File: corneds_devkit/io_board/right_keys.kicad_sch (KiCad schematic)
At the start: 42 parts, among them SW14 SW_Push, SW16 SW_Push, SW18 SW_Push, SW25 SW_Push, SW26 SW_Push, SW27 SW_Push, SW28 SW_Push, SW29 SW_Push, SW30 SW_Push, SW31 SW_Push, SW32 SW_Push, SW33 SW_Push, SW34 SW_Push, SW35 SW_Push, SW36 SW_Push, SW37 SW_Push, SW38 SW_Push, SW39 SW_Push, SW40 SW_Push, SW41 SW_Push, SW42 SW_Push

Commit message: routing left keys pcb
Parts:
- SW14, SW16, SW18, SW25, SW26, SW27, SW28, SW29, SW30, SW31, SW32, SW33, SW34, SW35, SW36, SW37, SW38, SW39, SW40, SW41, SW42: footprint key-switches:SW_Gateron_LowProfile_HotSwap_THT -> key-switches:SW_Gateron_LowProfile_HotSwap_PTH
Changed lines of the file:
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@@
 			)
 		)
-		(property "Footprint" "key-switches:SW_Gateron_LowProfile_HotSwap_THT"
+		(property "Footprint" "key-switches:SW_Gateron_LowProfile_HotSwap_PTH"
 			(at 128.27 34.29 0)
 			(effects
@@
 			)
 		)
-		(property "Footprint" "key-switches:SW_Gateron_LowProfile_HotSwap_THT"
+		(property "Footprint" "key-switches:SW_Gateron_LowProfile_HotSwap_PTH"
 			(at 100.33 130.81 0)
 			(effects
@@
 			)
 		)
-		(property "Footprint" "key-switches:SW_Gateron_LowProfile_HotSwap_THT"
+		(property "Footprint" "key-switches:SW_Gateron_LowProfile_HotSwap_PTH"
 			(at 72.39 34.29 0)
 			(effects
@@
 			)
 		)
-		(property "Footprint" "key-switches:SW_Gateron_LowProfile_HotSwap_THT"
+		(property "Footprint" "key-switches:SW_Gateron_LowProfile_HotSwap_PTH"
 			(at 72.39 99.06 0)
 			(effects
@@
 			)
 		)
-		(property "Footprint" "key-switches:SW_Gateron_LowProfile_HotSwap_THT"
+		(property "Footprint" "key-switches:SW_Gateron_LowProfile_HotSwap_PTH"
 			(at 156.21 34.29 0)
 			(effects
@@
 			)
 		)
-		(property "Footprint" "key-switches:SW_Gateron_LowProfile_HotSwap_THT"
+		(property "Footprint" "key-switches:SW_Gateron_LowProfile_HotSwap_PTH"
 			(at 100.33 66.04 0)
 			(effects
@@
 			)
 		)
-		(property "Footprint" "key-switches:SW_Gateron_LowProfile_HotSwap_THT"
+		(property "Footprint" "key-switches:SW_Gateron_LowProfile_HotSwap_PTH"
 			(at 128.27 66.04 0)
 			(effects
@@
 			)
 		)
-		(property "Footprint" "key-switches:SW_Gateron_LowProfile_HotSwap_THT"
+		(property "Footprint" "key-switches:SW_Gateron_LowProfile_HotSwap_PTH"
 			(at 100.33 99.06 0)
 			(effects
@@
 			)
 		)
-		(property "Footprint" "key-switches:SW_Gateron_LowProfile_HotSwap_THT"
+		(property "Footprint" "key-switches:SW_Gateron_LowProfile_HotSwap_PTH"
 			(at 212.09 34.29 0)
 			(effects
@@
 			)
 		)
-		(property "Footprint" "key-switches:SW_Gateron_LowProfile_HotSwap_THT"
+		(property "Footprint" "key-switches:SW_Gateron_LowProfile_HotSwap_PTH"
 			(at 212.09 99.06 0)
 			(effects
@@
 			)
 		)
-		(property "Footprint" "key-switches:SW_Gateron_LowProfile_HotSwap_THT"
+		(property "Footprint" "key-switches:SW_Gateron_LowProfile_HotSwap_PTH"
 			(at 184.15 99.06 0)
 			(effects
@@
 			)
 		)
-		(property "Footprint" "key-switches:SW_Gateron_LowProfile_HotSwap_THT"
+		(property "Footprint" "key-switches:SW_Gateron_LowProfile_HotSwap_PTH"
 			(at 128.27 99.06 0)
 			(effects
@@
 			)
 		)
-		(property "Footprint" "key-switches:SW_Gateron_LowProfile_HotSwap_THT"
+		(property "Footprint" "key-switches:SW_Gateron_LowProfile_HotSwap_PTH"
 			(at 184.15 34.29 0)
 			(effects
@@
 			)
 		)
-		(property "Footprint" "key-switches:SW_Gateron_LowProfile_HotSwap_THT"
+		(property "Footprint" "key-switches:SW_Gateron_LowProfile_HotSwap_PTH"
 			(at 212.09 66.04 0)
 			(effects
@@
 			)
 		)
-		(property "Footprint" "key-switches:SW_Gateron_LowProfile_HotSwap_THT"
+		(property "Footprint" "key-switches:SW_Gateron_LowProfile_HotSwap_PTH"
 			(at 100.33 34.29 0)
 			(effects
@@
 			)
 		)
-		(property "Footprint" "key-switches:SW_Gateron_LowProfile_HotSwap_THT"
+		(property "Footprint" "key-switches:SW_Gateron_LowProfile_HotSwap_PTH"
 			(at 184.15 66.04 0)
 			(effects
@@
 			)
 		)
-		(property "Footprint" "key-switches:SW_Gateron_LowProfile_HotSwap_THT"
+		(property "Footprint" "key-switches:SW_Gateron_LowProfile_HotSwap_PTH"
 			(at 128.27 130.81 0)
 			(effects
@@
 			)
 		)
-		(property "Footprint" "key-switches:SW_Gateron_LowProfile_HotSwap_THT"
+		(property "Footprint" "key-switches:SW_Gateron_LowProfile_HotSwap_PTH"
 			(at 156.21 99.06 0)
 			(effects
@@
 			)
 		)
-		(property "Footprint" "key-switches:SW_Gateron_LowProfile_HotSwap_THT"
+		(property "Footprint" "key-switches:SW_Gateron_LowProfile_HotSwap_PTH"
 			(at 72.39 130.81 0)
 			(effects
@@
 			)
 		)
-		(property "Footprint" "key-switches:SW_Gateron_LowProfile_HotSwap_THT"
+		(property "Footprint" "key-switches:SW_Gateron_LowProfile_HotSwap_PTH"
 			(at 72.39 66.04 0)
 			(effects
@@
 			)
 		)
-		(property "Footprint" "key-switches:SW_Gateron_LowProfile_HotSwap_THT"
+		(property "Footprint" "key-switches:SW_Gateron_LowProfile_HotSwap_PTH"
 			(at 156.21 66.04 0)
 			(effects

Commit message: finished io board
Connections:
- net rclick_led_di: now also D78.1 (DO); no longer D64.1 (DO)
- net right_led_di: now also D77.4 (DI); no longer D26.4 (DI)
- net at D79.1 (DO): now also D71.4 (DI); no longer D80.4 (DI)
- net at D71.1 (DO): now also D63.4 (DI); no longer D79.4 (DI)
- net at D72.1 (DO): now also D80.4 (DI); no longer D64.4 (DI)
- net at D72.4 (DI): now also D64.1 (DO); no longer D80.1 (DO)
- net at D50.1 (DO): now also D56.4 (DI); no longer D28.4 (DI)
- net at D50.4 (DI): now also D28.1 (DO); no longer D56.1 (DO)
- net at D30.4 (DI): now also D51.1 (DO); no longer D28.1 (DO)
- net at D63.1 (DO): now also D57.4 (DI); no longer D71.4 (DI)
- net at D57.1 (DO): now also D51.4 (DI); no longer D63.4 (DI)
- net at D70.4 (DI): now also D62.1 (DO); no longer D78.1 (DO)
- net at D78.4 (DI): now also D70.1 (DO); no longer D77.1 (DO)
- net at D61.1 (DO): now also D55.4 (DI); no longer D69.4 (DI)
- net at D61.4 (DI): now also D69.1 (DO); no longer D55.1 (DO)
- net at D49.1 (DO): now also D26.4 (DI); no longer D55.4 (DI)
- net at D26.1 (DO): now also D28.4 (DI); no longer D49.4 (DI)
- net at D30.1 (DO): now also D64.4 (DI); no longer D51.4 (DI)
- net at D62.4 (DI): now also D56.1 (DO); no longer D70.1 (DO)
- new net: D69.4 (DI), D77.1 (DO)
- new net: D49.4 (DI), D55.1 (DO)
- new net rclick_led_do: D79.4 (DI)

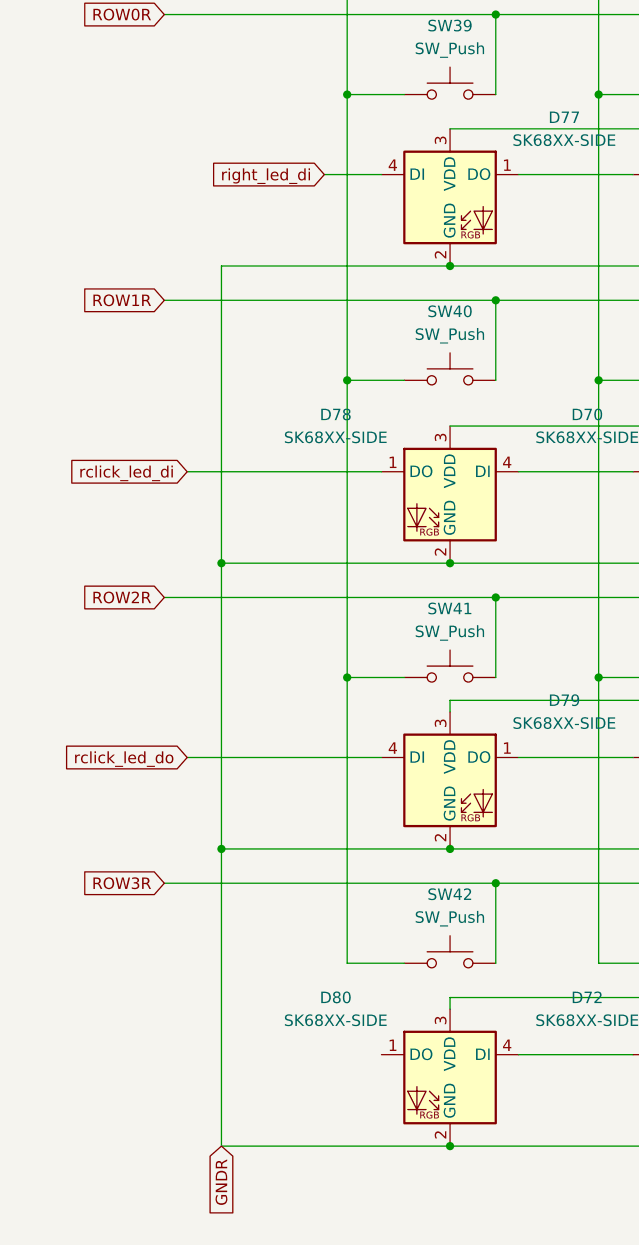
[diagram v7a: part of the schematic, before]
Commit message: finished routing power board and started on control board schematic but realized I need seperate reset lines
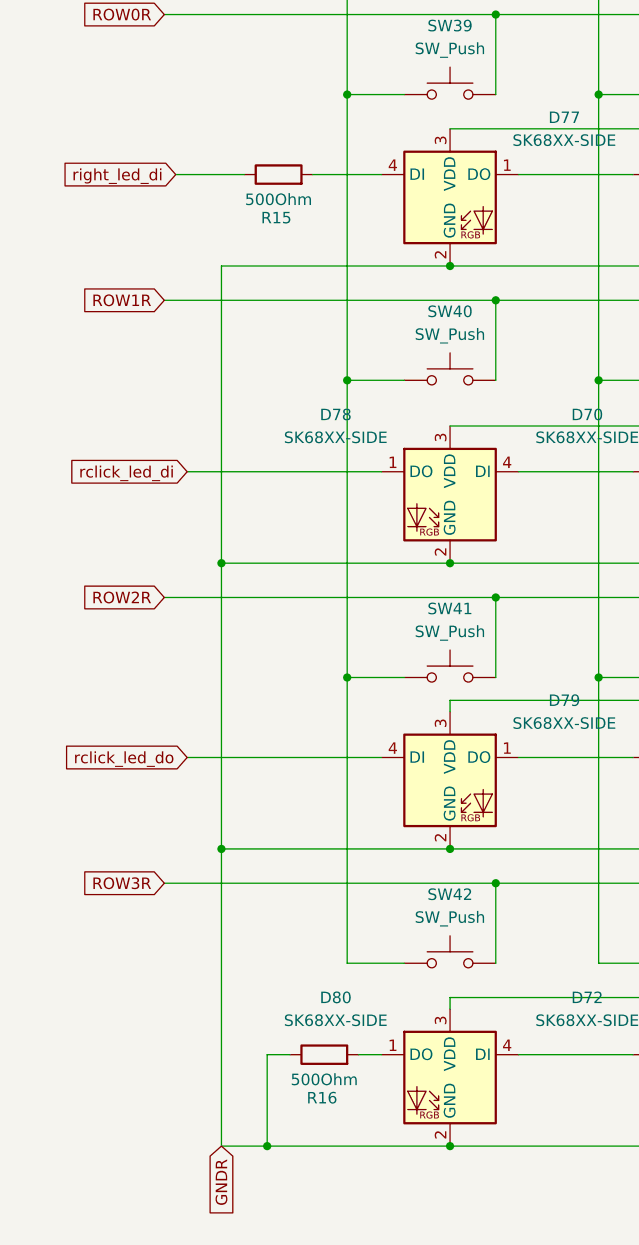
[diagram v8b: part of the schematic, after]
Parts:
- added R15, R16: 500Ohm, Resistor_SMD:R_0402_1005Metric, symbol Device:R
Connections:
- net GNDR: now also R16.1
- net right_led_di: now also R15.1; no longer D77.4 (DI)
- net at D80.1 (DO): now also R16.2
- new net: D77.4 (DI), R15.2
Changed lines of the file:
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@@
 	)
 	(junction
+		(at 52.07 156.21)
+		(diameter 0)
+		(color 0 0 0 0)
+	)
+	(junction
 		(at 128.27 91.44)
 		(diameter 0)
@@
 	(wire
 		(pts
-			(xy 72.39 156.21) (xy 46.99 156.21)
+			(xy 72.39 156.21) (xy 52.07 156.21)
 		)
 		(stroke
@@
 	(wire
 		(pts
+			(xy 62.23 146.05) (xy 64.77 146.05)
+		)
+		(stroke
+			(width 0)
+			(type default)
+		)
+	)
+	(wire
+		(pts
 			(xy 224.79 48.26) (xy 219.71 48.26)
 		)
@@
 	(wire
 		(pts
-			(xy 40.64 127) (xy 77.47 127)
+			(xy 52.07 146.05) (xy 52.07 156.21)
 		)
 		(stroke
@@
 	(wire
 		(pts
-			(xy 133.35 62.23) (xy 161.29 62.23)
+			(xy 40.64 127) (xy 77.47 127)
 		)
 		(stroke
@@
 	(wire
 		(pts
-			(xy 207.01 104.14) (xy 203.2 104.14)
+			(xy 133.35 62.23) (xy 161.29 62.23)
 		)
 		(stroke
@@
 	(wire
 		(pts
-			(xy 173.99 71.12) (xy 173.99 39.37)
+			(xy 207.01 104.14) (xy 203.2 104.14)
 		)
 		(stroke
@@
 	(wire
 		(pts
-			(xy 189.23 71.12) (xy 189.23 62.23)
+			(xy 173.99 71.12) (xy 173.99 39.37)
 		)
 		(stroke
@@
 	(wire
 		(pts
-			(xy 46.99 91.44) (xy 46.99 58.42)
+			(xy 189.23 71.12) (xy 189.23 62.23)
 		)
 		(stroke
@@
 	(wire
 		(pts
-			(xy 58.42 48.26) (xy 64.77 48.26)
+			(xy 46.99 91.44) (xy 46.99 58.42)
 		)
 		(stroke
@@
 	(wire
 		(pts
+			(xy 41.91 48.26) (xy 49.53 48.26)
+		)
+		(stroke
+			(width 0)
+			(type default)
+		)
+	)
+	(wire
+		(pts
 			(xy 72.39 139.7) (xy 72.39 140.97)
 		)
@@
 	(wire
 		(pts
+			(xy 57.15 48.26) (xy 64.77 48.26)
+		)
+		(stroke
+			(width 0)
+			(type default)
+		)
+	)
+	(wire
+		(pts
 			(xy 77.47 62.23) (xy 105.41 62.23)
 		)
@@
 	(wire
 		(pts
+			(xy 52.07 156.21) (xy 46.99 156.21)
+		)
+		(stroke
+			(width 0)
+			(type default)
+		)
+	)
+	(wire
+		(pts
 			(xy 100.33 123.19) (xy 72.39 123.19)
 		)
@@
 	(wire
 		(pts
+			(xy 54.61 146.05) (xy 52.07 146.05)
+		)
+		(stroke
+			(width 0)
+			(type default)
+		)
+	)
+	(wire
+		(pts
 			(xy 189.23 104.14) (xy 189.23 95.25)
 		)
@@
 	(global_label "right_led_di"
 		(shape input)
-		(at 58.42 48.26 180)
+		(at 41.91 48.26 180)
 		(fields_autoplaced yes)
 		(effects
@@
 		)
 		(property "Intersheetrefs" "${INTERSHEET_REFS}"
-			(at 44.4283 48.26 0)
+			(at 27.9183 48.26 0)
 			(effects
 				(font
@@
 	)
 	(symbol
+		(lib_id "Device:R")
+		(at 58.42 146.05 90)
+		(unit 1)
+		(exclude_from_sim no)
+		(in_bom yes)
+		(on_board yes)
+		(dnp no)
+		(property "Reference" "R16"
+			(at 58.166 150.876 90)
+			(effects
+				(font
+					(size 1.27 1.27)
+				)
+			)
+		)
+		(property "Value" "500Ohm"
+			(at 58.42 148.844 90)
+			(effects
+				(font
+					(size 1.27 1.27)
+				)
+			)
+		)
+		(property "Footprint" "Resistor_SMD:R_0402_1005Metric"
+			(at 58.42 147.828 90)
+			(effects
+				(font
+					(size 1.27 1.27)
+				)
+				(hide yes)
+			)
+		)
+		(property "Datasheet" "~"
+			(at 58.42 146.05 0)
+			(effects
+				(font
+					(size 1.27 1.27)
+				)
+				(hide yes)
+			)
+		)
+		(property "Description" "Resistor"
+			(at 58.42 146.05 0)
+			(effects
+				(font
+					(size 1.27 1.27)
+				)
+				(hide yes)
+			)
+		)
+		(pin "1"
+		)
+		(pin "2"
+		)
+		(instances
+			(project "io_board"
+				(path "/244b6d6b-132d-4d50-ae86-e41103b29008/bd07eb4f-2b61-4923-a58a-bccd1af7bd24"
+					(reference "R16")
+					(unit 1)
+				)
+			)
+		)
+	)
+	(symbol
 		(lib_id "LED:APA-106-F5")
 		(at 72.39 83.82 0)
@@
 					(unit 1)
 				)
+			)
+		)
+	)
+	(symbol
+		(lib_id "Device:R")
+		(at 53.34 48.26 90)
+		(unit 1)
+		(exclude_from_sim no)
+		(in_bom yes)
+		(on_board yes)
+		(dnp no)
+		(property "Reference" "R15"
+			(at 53.086 53.086 90)
+			(effects
+				(font
+					(size 1.27 1.27)
+				)
+			)
+		)
+		(property "Value" "500Ohm"
+			(at 53.34 51.054 90)
+			(effects
+				(font
+					(size 1.27 1.27)
+				)
+			)
+		)
+		(property "Footprint" "Resistor_SMD:R_0402_1005Metric"
+			(at 53.34 50.038 90)
+			(effects
+				(font
+					(size 1.27 1.27)
+				)
+				(hide yes)
+			)
+		)
+		(property "Datasheet" "~"
+			(at 53.34 48.26 0)
+			(effects
+				(font
+					(size 1.27 1.27)
+				)
+				(hide yes)
+			)
+		)
+		(property "Description" "Resistor"
+			(at 53.34 48.26 0)
+			(effects
+				(font
+					(size 1.27 1.27)
+				)
+				(hide yes)
+			)
+		)
+		(pin "1"
+		)
+		(pin "2"
+		)
+		(instances
+			(project "io_board"
+				(path "/244b6d6b-132d-4d50-ae86-e41103b29008/bd07eb4f-2b61-4923-a58a-bccd1af7bd24"
+					(reference "R15")
+					(unit 1)
+				)
